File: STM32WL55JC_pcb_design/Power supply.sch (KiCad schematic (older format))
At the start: 14 parts, among them J17 CT3151-2, J18 CT3151-2, J19 USB_A, J20 Conn_02x02_Odd_Even, Q1 AO3401A, U6 AMS1117-3.3, U7 AMS1117-5.0

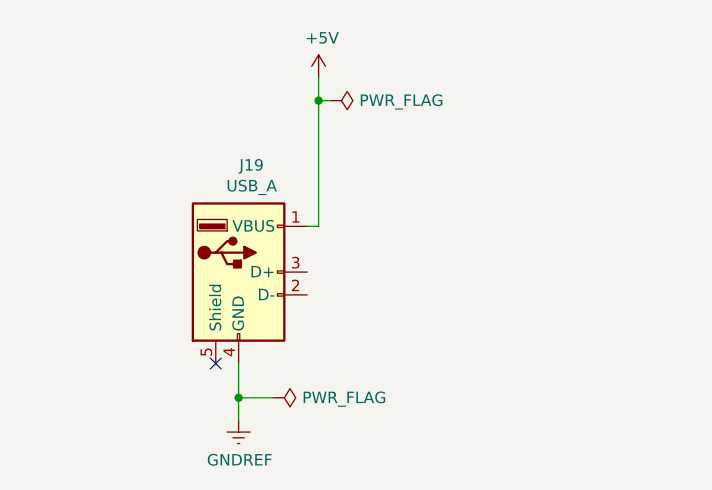
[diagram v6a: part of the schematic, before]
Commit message: Initial pcb layout
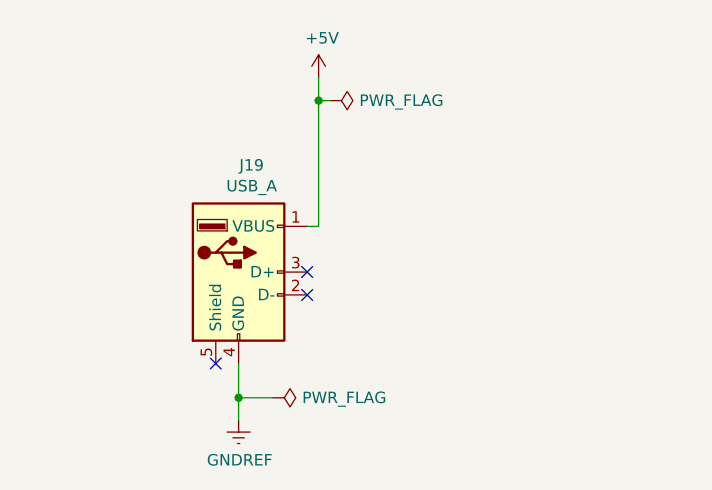
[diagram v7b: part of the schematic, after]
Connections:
- no-connect marks 1 -> 3
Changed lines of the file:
@@
 Wire Wire Line
 	6050 2500 6200 2500
+NoConn ~ 3750 5100
+NoConn ~ 3750 5000
 $EndSCHEMATC

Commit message: Finish new design schematic
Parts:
- renumbered C48 to C61, C50 to C62, C51 to C63, C52 to C64, J17 to J18, J18 to J19, J19 to J20, J20 to J21, R11 to R12, U6 to U4, U7 to U5
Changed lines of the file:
@@
 $EndDescr
 $Comp
-L Device:C C48
+L Device:C C61
 U 1 1 612D3281
 P 6200 2800
-F 0 "C48" H 6315 2846 50  0000 L CNN
+F 0 "C61" H 6315 2846 50  0000 L CNN
 F 1 "10uF" H 6315 2755 50  0000 L CNN
 F 2 "Capacitor_SMD:C_0805_2012Metric" H 6238 2650 50  0001 C CNN
@@
 $EndComp
 $Comp
-L Device:C C51
+L Device:C C63
 U 1 1 612D3287
 P 7950 2800
-F 0 "C51" H 8065 2846 50  0000 L CNN
+F 0 "C63" H 8065 2846 50  0000 L CNN
 F 1 "10uF" H 8065 2755 50  0000 L CNN
 F 2 "Capacitor_SMD:C_0805_2012Metric" H 7988 2650 50  0001 C CNN
@@
 $EndComp
 $Comp
-L power:PWR_FLAG #FLG0101
+L power:PWR_FLAG #FLG01
 U 1 1 612D329C
 P 3400 2650
-F 0 "#FLG0101" H 3400 2725 50  0001 C CNN
+F 0 "#FLG01" H 3400 2725 50  0001 C CNN
 F 1 "PWR_FLAG" V 3400 2778 50  0000 L CNN
 F 2 "" H 3400 2650 50  0001 C CNN
@@
 $EndComp
 $Comp
-L power:PWR_FLAG #FLG0102
+L power:PWR_FLAG #FLG02
 U 1 1 612D32A2
 P 3400 3250
-F 0 "#FLG0102" H 3400 3325 50  0001 C CNN
+F 0 "#FLG02" H 3400 3325 50  0001 C CNN
 F 1 "PWR_FLAG" V 3400 3378 50  0000 L CNN
 F 2 "" H 3400 3250 50  0001 C CNN
@@
 	3350 3250 3350 3300
 $Comp
-L Device:R R11
+L Device:R R12
 U 1 1 612D32AE
 P 4900 3050
-F 0 "R11" H 4970 3096 50  0000 L CNN
+F 0 "R12" H 4970 3096 50  0000 L CNN
 F 1 "100kOhm" H 4970 3005 50  0000 L CNN
 F 2 "Resistor_SMD:R_0805_2012Metric" V 4830 3050 50  0001 C CNN
@@
 	7950 2500 7950 2650
 $Comp
-L STM32WL55JC_pcb_design-rescue:CT3151-2-CT3151-2 J17
+L STM32WL55JC_pcb_design-rescue:CT3151-2-CT3151-2 J18
 U 1 1 612D4BF0
 P 3050 2900
-F 0 "J17" H 3180 2946 50  0000 L CNN
+F 0 "J18" H 3180 2946 50  0000 L CNN
 F 1 "CT3151-2" H 3180 2855 50  0000 L CNN
 F 2 "CT3151-2:CALTEST_CT3151-2" H 3050 2900 50  0001 L BNN
@@
 $EndComp
 $Comp
-L STM32WL55JC_pcb_design-rescue:CT3151-2-CT3151-2 J18
+L STM32WL55JC_pcb_design-rescue:CT3151-2-CT3151-2 J19
 U 1 1 612D8B84
 P 3050 3150
-F 0 "J18" H 3180 3196 50  0000 L CNN
+F 0 "J19" H 3180 3196 50  0000 L CNN
 F 1 "CT3151-2" H 3180 3105 50  0000 L CNN
 F 2 "CT3151-2:CALTEST_CT3151-2" H 3050 3150 50  0001 L BNN
@@
 AR Path="/612E8262" Ref="#PWR?"  Part="1"
 AR Path="/612ED5EB/612E8262" Ref="#PWR?"  Part="1"
-AR Path="/612BE788/612E8262" Ref="#PWR0157"  Part="1"
-F 0 "#PWR0157" H 3350 3050 50  0001 C CNN
+AR Path="/612BE788/612E8262" Ref="#PWR077"  Part="1"
+F 0 "#PWR077" H 3350 3050 50  0001 C CNN
 F 1 "GNDREF" H 3355 3127 50  0000 C CNN
 F 2 "" H 3350 3300 50  0001 C CNN
@@
 AR Path="/612EB197" Ref="#PWR?"  Part="1"
 AR Path="/612ED5EB/612EB197" Ref="#PWR?"  Part="1"
-AR Path="/612BE788/612EB197" Ref="#PWR0158"  Part="1"
-F 0 "#PWR0158" H 4900 3050 50  0001 C CNN
+AR Path="/612BE788/612EB197" Ref="#PWR081"  Part="1"
+F 0 "#PWR081" H 4900 3050 50  0001 C CNN
 F 1 "GNDREF" H 4905 3127 50  0000 C CNN
 F 2 "" H 4900 3300 50  0001 C CNN
@@
 AR Path="/612EBFE1" Ref="#PWR?"  Part="1"
 AR Path="/612ED5EB/612EBFE1" Ref="#PWR?"  Part="1"
-AR Path="/612BE788/612EBFE1" Ref="#PWR0159"  Part="1"
-F 0 "#PWR0159" H 7150 2750 50  0001 C CNN
+AR Path="/612BE788/612EBFE1" Ref="#PWR082"  Part="1"
+F 0 "#PWR082" H 7150 2750 50  0001 C CNN
 F 1 "GNDREF" H 7155 2827 50  0000 C CNN
 F 2 "" H 7150 3000 50  0001 C CNN
@@
 AR Path="/613F6531" Ref="#PWR?"  Part="1"
 AR Path="/612ED5EB/613F6531" Ref="#PWR?"  Part="1"
-AR Path="/612BE788/613F6531" Ref="#PWR0160"  Part="1"
-F 0 "#PWR0160" H 4200 2750 50  0001 C CNN
+AR Path="/612BE788/613F6531" Ref="#PWR080"  Part="1"
+F 0 "#PWR080" H 4200 2750 50  0001 C CNN
 F 1 "+5V" H 4215 3073 50  0000 C CNN
 F 2 "" H 4200 2900 50  0001 C CNN
@@
 Connection ~ 5200 2500
 $Comp
-L Connector_Generic:Conn_02x02_Odd_Even J20
+L Connector_Generic:Conn_02x02_Odd_Even J21
 U 1 1 612F9E39
 P 4250 2500
-F 0 "J20" H 4300 2717 50  0000 C CNN
+F 0 "J21" H 4300 2717 50  0000 C CNN
 F 1 "Conn_02x02_Odd_Even" H 4300 2626 50  0000 C CNN
 F 2 "Connector_PinHeader_2.54mm:PinHeader_2x02_P2.54mm_Vertical_SMD" H 4250 2500 50  0001 C CNN
@@
 	6200 1500 6400 1500
 $Comp
-L Device:C C50
+L Device:C C62
 U 1 1 6138C044
 P 6400 1750
-F 0 "C50" H 6515 1796 50  0000 L CNN
+F 0 "C62" H 6515 1796 50  0000 L CNN
 F 1 "10uF" H 6515 1705 50  0000 L CNN
 F 2 "Capacitor_SMD:C_0805_2012Metric" H 6438 1600 50  0001 C CNN
@@
 Connection ~ 6400 1500
 $Comp
-L Device:C C52
+L Device:C C64
 U 1 1 6138F7A9
 P 8000 1750
-F 0 "C52" H 8115 1796 50  0000 L CNN
+F 0 "C64" H 8115 1796 50  0000 L CNN
 F 1 "10uF" H 8115 1705 50  0000 L CNN
 F 2 "Capacitor_SMD:C_0805_2012Metric" H 8038 1600 50  0001 C CNN
@@
 AR Path="/6139377B" Ref="#PWR?"  Part="1"
 AR Path="/612ED5EB/6139377B" Ref="#PWR?"  Part="1"
-AR Path="/612BE788/6139377B" Ref="#PWR0161"  Part="1"
-F 0 "#PWR0161" H 7200 1750 50  0001 C CNN
+AR Path="/612BE788/6139377B" Ref="#PWR083"  Part="1"
+F 0 "#PWR083" H 7200 1750 50  0001 C CNN
 F 1 "GNDREF" H 7205 1827 50  0000 C CNN
 F 2 "" H 7200 2000 50  0001 C CNN
@@
 AR Path="/61575FBB" Ref="J?"  Part="1"
 AR Path="/612ED5EB/61575FBB" Ref="J?"  Part="1"
-AR Path="/612BE788/61575FBB" Ref="J19"  Part="1"
+AR Path="/612BE788/61575FBB" Ref="J20"  Part="1"
 AR Path="/616239B7/61575FBB" Ref="J?"  Part="1"
-F 0 "J19" H 3507 5467 50  0000 C CNN
+F 0 "J20" H 3507 5467 50  0000 C CNN
 F 1 "USB_A" H 3507 5376 50  0000 C CNN
 F 2 "USBASFBTH:USBASFBTH" H 3600 4950 50  0001 C CNN
@@
 AR Path="/61575FCF" Ref="#PWR?"  Part="1"
 AR Path="/612ED5EB/61575FCF" Ref="#PWR?"  Part="1"
-AR Path="/612BE788/61575FCF" Ref="#PWR0162"  Part="1"
+AR Path="/612BE788/61575FCF" Ref="#PWR078"  Part="1"
 AR Path="/616239B7/61575FCF" Ref="#PWR?"  Part="1"
-F 0 "#PWR0162" H 3450 5400 50  0001 C CNN
+F 0 "#PWR078" H 3450 5400 50  0001 C CNN
 F 1 "GNDREF" H 3455 5477 50  0000 C CNN
 F 2 "" H 3450 5650 50  0001 C CNN
@@
 AR Path="/61575FD6" Ref="#PWR?"  Part="1"
 AR Path="/612ED5EB/61575FD6" Ref="#PWR?"  Part="1"
-AR Path="/612BE788/61575FD6" Ref="#PWR0163"  Part="1"
+AR Path="/612BE788/61575FD6" Ref="#PWR079"  Part="1"
 AR Path="/616239B7/61575FD6" Ref="#PWR?"  Part="1"
-F 0 "#PWR0163" H 3800 4000 50  0001 C CNN
+F 0 "#PWR079" H 3800 4000 50  0001 C CNN
 F 1 "+5V" H 3815 4323 50  0000 C CNN
 F 2 "" H 3800 4150 50  0001 C CNN
@@
 AR Path="/61575FEE" Ref="#FLG?"  Part="1"
 AR Path="/612ED5EB/61575FEE" Ref="#FLG?"  Part="1"
-AR Path="/612BE788/61575FEE" Ref="#FLG0103"  Part="1"
+AR Path="/612BE788/61575FEE" Ref="#FLG04"  Part="1"
 AR Path="/616239B7/61575FEE" Ref="#FLG?"  Part="1"
-F 0 "#FLG0103" H 3850 4325 50  0001 C CNN
+F 0 "#FLG04" H 3850 4325 50  0001 C CNN
 F 1 "PWR_FLAG" V 3850 4378 50  0000 L CNN
 F 2 "" H 3850 4250 50  0001 C CNN
@@
 AR Path="/61575FF4" Ref="#FLG?"  Part="1"
 AR Path="/612ED5EB/61575FF4" Ref="#FLG?"  Part="1"
-AR Path="/612BE788/61575FF4" Ref="#FLG0104"  Part="1"
+AR Path="/612BE788/61575FF4" Ref="#FLG03"  Part="1"
 AR Path="/616239B7/61575FF4" Ref="#FLG?"  Part="1"
-F 0 "#FLG0104" H 3600 5625 50  0001 C CNN
+F 0 "#FLG03" H 3600 5625 50  0001 C CNN
 F 1 "PWR_FLAG" V 3600 5678 50  0000 L CNN
 F 2 "" H 3600 5550 50  0001 C CNN
@@
 	7950 3000 8500 3000
 $Comp
-L Regulator_Linear:AMS1117-3.3 U6
+L Regulator_Linear:AMS1117-3.3 U4
 U 1 1 617E4B61
 P 7150 2500
-F 0 "U6" H 7150 2742 50  0000 C CNN
+F 0 "U4" H 7150 2742 50  0000 C CNN
 F 1 "AMS1117-3.3" H 7150 2651 50  0000 C CNN
 F 2 "Package_TO_SOT_SMD:SOT-223-3_TabPin2" H 7150 2700 50  0001 C CNN
@@
 	7150 2800 7150 3000
 $Comp
-L Regulator_Linear:AMS1117-5.0 U7
+L Regulator_Linear:AMS1117-5.0 U5
 U 1 1 617ED585
 P 7200 1500
-F 0 "U7" H 7200 1742 50  0000 C CNN
+F 0 "U5" H 7200 1742 50  0000 C CNN
 F 1 "AMS1117-5.0" H 7200 1651 50  0000 C CNN
 F 2 "Package_TO_SOT_SMD:SOT-223-3_TabPin2" H 7200 1700 50  0001 C CNN
